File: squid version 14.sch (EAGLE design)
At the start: 61 parts, among them J2 ATMEL_PROGRAMMER_HEADERNL, U2 MCP73832

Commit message: add label
minor change
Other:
- note added: "Schottky diode or a jumper"
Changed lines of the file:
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@@
 <text x="109.22" y="190.5" size="1.778" layer="91">RESET LOW when charging</text>
 <text x="330.2" y="167.64" size="1.778" layer="94">Use a Resistor Array instead of discrete chips</text>
+<text x="-7.62" y="160.02" size="1.778" layer="94">Schottky diode or a jumper</text>
 </plain>
 <instances>

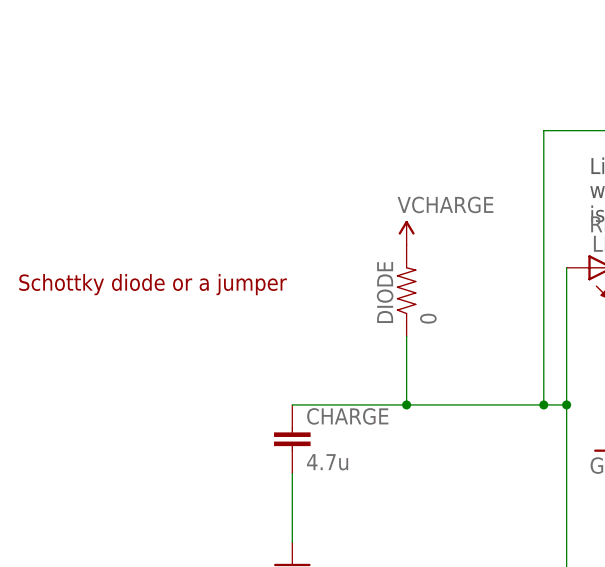
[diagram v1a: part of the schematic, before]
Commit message: added some comments
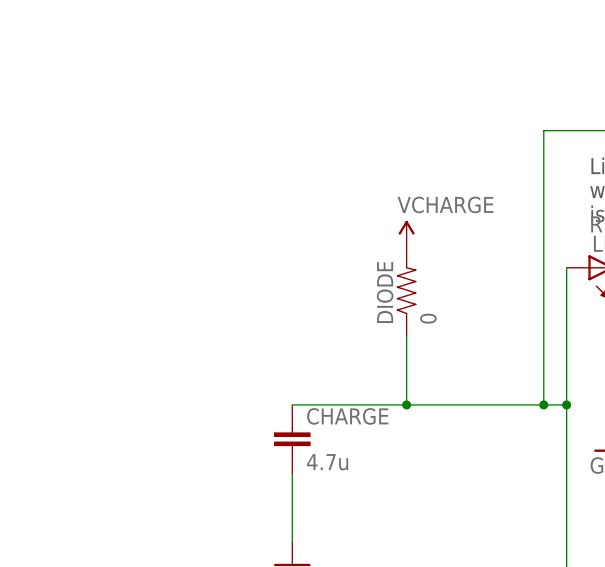
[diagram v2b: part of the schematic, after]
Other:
- note removed: "Schottky diode or a jumper"
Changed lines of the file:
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@@
 <text x="109.22" y="190.5" size="1.778" layer="91">RESET LOW when charging</text>
 <text x="330.2" y="167.64" size="1.778" layer="94">Use a Resistor Array instead of discrete chips</text>
-<text x="-7.62" y="160.02" size="1.778" layer="94">Schottky diode or a jumper</text>
 </plain>
 <instances>
